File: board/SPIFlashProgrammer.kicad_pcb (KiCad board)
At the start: 4 copper layers, 54.3 x 24 mm, 63 parts, among them J1 Conn_02x04_Counter_Clockwise, J2 Conn_02x05_Odd_Even, Q1 DMN65D8L-7, Q2 DMN65D8L-7, Q3 2N7002DW, Q4 DMN65D8L-7, SW1 B3U-1000P-B, SW2 B3U-1000P-B, U1 TM4C123GH6PM, U2 FXL4TD245BQX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

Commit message: KiCad file updates
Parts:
- added SYM2: SYM_ESD_Small, Symbol:ESD-Logo_6.6x6mm_SilkScreen, F.Cu at (136.6, 93.1)
- D1: value D_Schottky_Small -> PMEG2010BELD,315
- R15: value 10k -> 1k
- R16: value 10k -> 750
- R18: value 10k -> 250
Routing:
- net /Onboard Flash/~CS2: track 33.4 -> 30.0 mm
- net /Onboard Flash/COPI: track 28.7 -> 29.2 mm
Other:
- outline, holes or cut-outs redrawn
- board text added: "CERN OHL v2 Strict"
- board text added: "SPIFlashProgrammer rev 2a"
- board text removed: "CERN OHL v1.2"
- board text removed: "SPIFlashProgrammer rev 2"

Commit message: Added a SPI present signal for the external bus to the CPU to make detection easier
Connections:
- Q2 pad 3: Net-(Q2-Pad3) -> /Connectors/~SPI_PRESENT
- R12 pad 2: Net-(Q2-Pad3) -> /Connectors/~SPI_PRESENT
- U1 pad 1: Net-(U1-Pad1) -> /Connectors/~SPI_PRESENT
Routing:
- net /Connectors/~SPI_PRESENT: track 0.00 -> 27.7 mm, vias 0 -> 2
- net Net-(Q2-Pad3): track 2.59 -> 0.00 mm

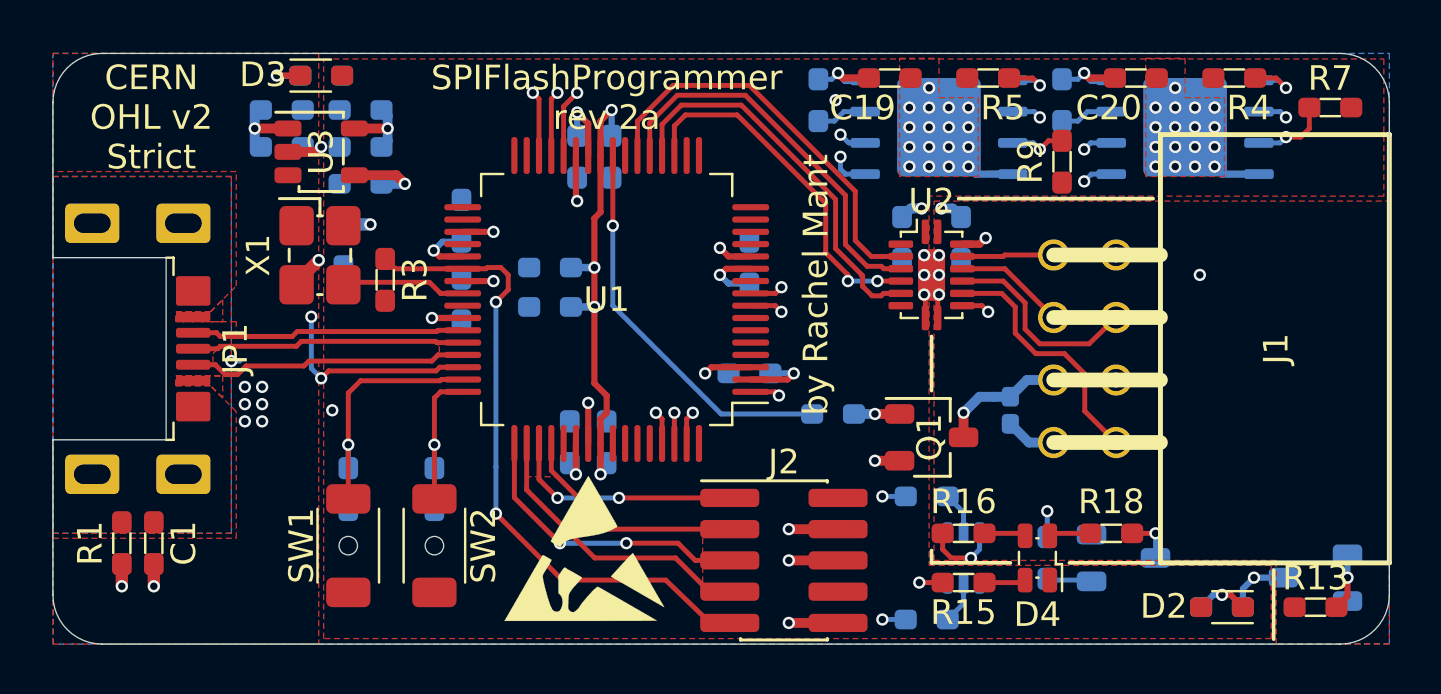
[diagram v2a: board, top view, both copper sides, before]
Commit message: Upgraded the KiCad files to v6 format
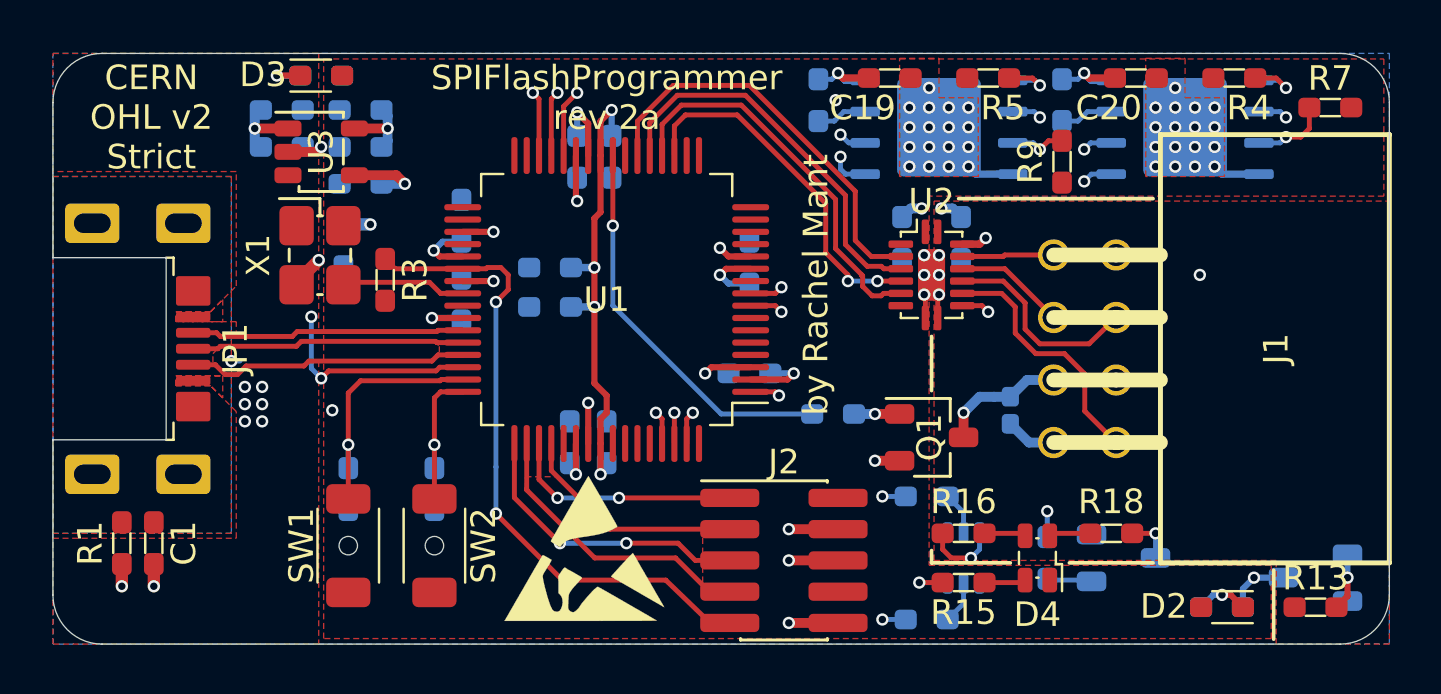
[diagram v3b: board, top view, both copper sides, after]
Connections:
- net /Connectors/~RESET renamed /Connectors/~{RESET}
- net /Connectors/~SCS renamed /Connectors/~{SCS}
- net /Connectors/~SPI_CS renamed /Connectors/~{SPI_CS}
- net /Connectors/~SPI_PRESENT renamed /Connectors/~{SPI_PRESENT}
- net /Connectors/~SRESET renamed /Connectors/~{SRESET}
- net /Connectors/~SRST renamed /Connectors/~{SRST}
- net /Onboard Flash/~CS1 renamed /Onboard Flash/~{CS1}
- net /Onboard Flash/~CS2 renamed /Onboard Flash/~{CS2}
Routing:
- added copper zone on In2.Cu, net +3V3
- added copper zone on In2.Cu, net /Connectors/SPI_VCC
- added copper zone on In2.Cu, net /Connectors/VBUS
- added copper zone on In1.Cu, net Earth
- added copper zone on In2.Cu, net Earth
- added copper zone on In1.Cu, net GND
- added copper zone on In2.Cu, net GND
- removed copper zone on Inner_2, net +3V3
- removed copper zone on Inner_2, net /Connectors/SPI_VCC
- removed copper zone on Inner_2, net /Connectors/VBUS
- removed copper zone on Inner_1, net Earth
- removed copper zone on Inner_2, net Earth
- removed copper zone on Inner_1, net GND
- removed copper zone on Inner_2, net GND
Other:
- net class Default removed
- board text added: "~CS"
- board text added: "~RESET"
- board text removed: "~~CS"
- board text removed: "~~RESET"
